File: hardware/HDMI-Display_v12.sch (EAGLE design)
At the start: 105 parts, among them IC1 TFP401A-PAD, IC2 24LC02B, IC3 IS31BL3506A-TTLS2, IC4 ATMEGA32U4-MU, IC5 VREG-TS1117CW-3V3, J20_1 JUMPER2-0402, J20_2 JUMPER2-0402, J30_1 JUMPER2-0402, J30_2 JUMPER2-0402, Q1 16MHz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

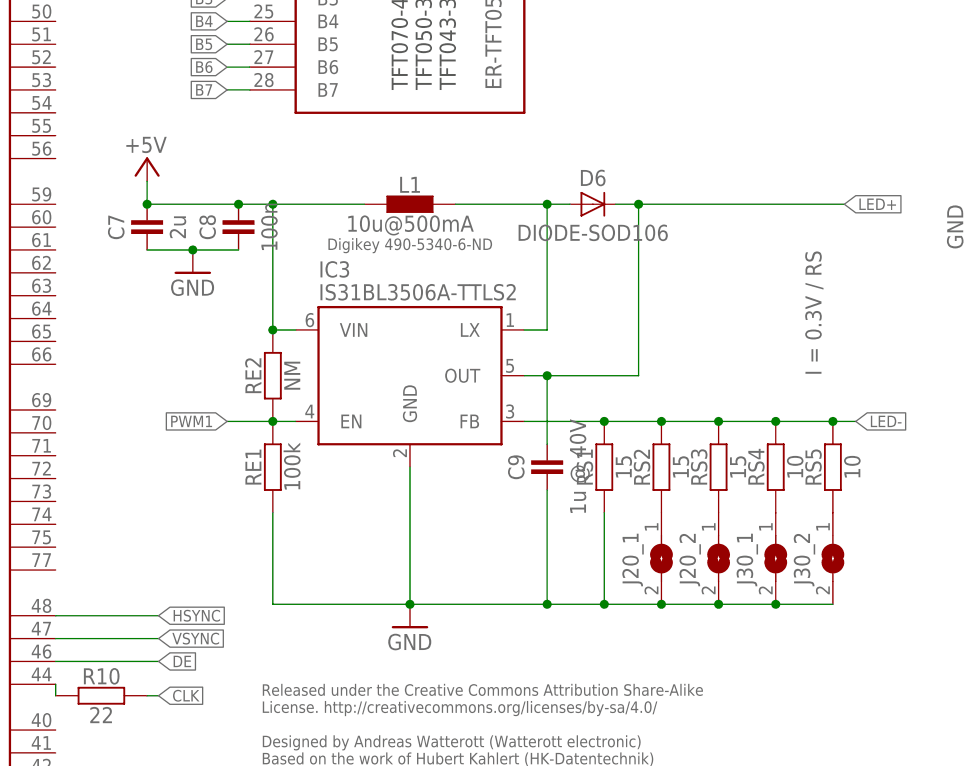
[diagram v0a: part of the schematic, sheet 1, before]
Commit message: updated schematics
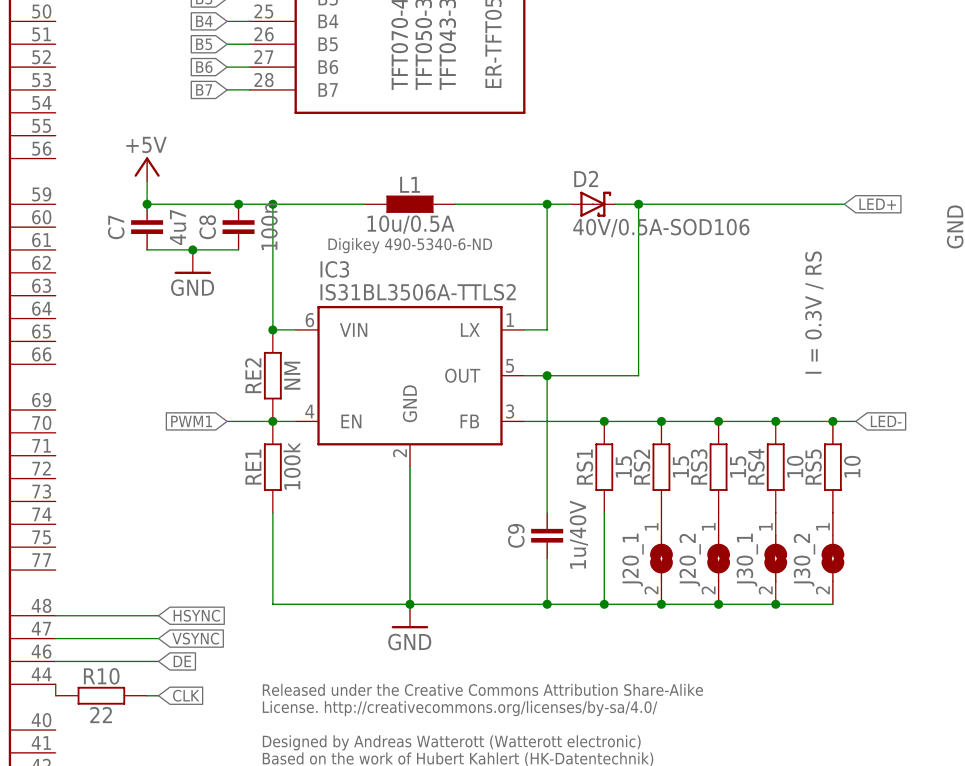
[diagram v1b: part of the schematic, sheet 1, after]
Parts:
- removed D6: DIODE-SOD106, we-rcl:DIODE-SOD106
- added D2: 40V/0.5A-SOD106, we-rcl:D_SCHOTTKY-SOD106
- C7: value 2u -> 4u7
- C9: value 1u @ 40V -> 1u/40V
- L1: value 10u@500mA -> 10u/0.5A
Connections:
- net LED+: now also D2.C; no longer D6.C
- net LX: now also D2.A; no longer D6.A
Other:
- note removed: "Based on the work of Hubert Kahlert (HK-Datentechnik)"
- note removed: "Designed by Andreas Watterott (Watterott electronic)"
- note removed: "Released under the Creative Commons Attribution Share-Alike License"
- note removed: "http://creativecommons.org/licenses/by-sa/4.0/"
- moved on the sheet: C9
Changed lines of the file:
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@@
 <part name="USB" library="we-con" deviceset="USB" device="-MICROB"/>
 <part name="IC3" library="we-power" deviceset="IS31BL3506A" device="-TTLS2"/>
-<part name="L1" library="we-power" deviceset="INDUCTOR" device="-1212" value="10u@500mA"/>
-<part name="D6" library="we-rcl" deviceset="DIODE" device="-SOD106" value="DIODE-SOD106"/>
+<part name="L1" library="we-power" deviceset="INDUCTOR" device="-1212" value="10u/0.5A"/>
 <part name="P+11" library="supply1" deviceset="+5V" device=""/>
 <part name="GND23" library="supply1" deviceset="GND" device=""/>
 <part name="RS2" library="we-rcl" deviceset="RESISTOR" device="-0402" value="15"/>
-<part name="C9" library="we-rcl" deviceset="CAPACITOR" device="-0805" value="1u @ 40V"/>
+<part name="C9" library="we-rcl" deviceset="CAPACITOR" device="-0805" value="1u/40V"/>
 <part name="ISP" library="we-board" deviceset="ISP" device=""/>
 <part name="LCD_TOP" library="we-opto" deviceset="ER-TFT" device="050-3"/>
@@
 <part name="GND9" library="supply1" deviceset="GND" device=""/>
 <part name="C8" library="we-rcl" deviceset="CAPACITOR" device="-0402" value="100n"/>
-<part name="C7" library="we-rcl" deviceset="CAPACITOR" device="-0402" value="2u"/>
+<part name="C7" library="we-rcl" deviceset="CAPACITOR" device="-0402" value="4u7"/>
 <part name="GND6" library="supply1" deviceset="GND" device=""/>
 <part name="RPI" library="we-con" deviceset="MA08-2" device=""/>
@@
 <part name="SW2" library="we-switch" deviceset="SW-2UM" device="-CUS22B"/>
 <part name="SW1" library="we-switch" deviceset="SW-TACTILE" device="-PTS840P"/>
+<part name="D2" library="we-rcl" deviceset="D_SCHOTTKY" device="-SOD106" value="40V/0.5A-SOD106"/>
 </parts>
 <sheets>
@@
 <instance part="IC3" gate="IC" x="179.07" y="57.15"/>
 <instance part="L1" gate="L" x="179.07" y="76.2"/>
-<instance part="D6" gate="D" x="199.39" y="76.2"/>
 <instance part="P+11" gate="1" x="149.86" y="81.28" smashed="yes">
 <attribute name="VALUE" x="147.32" y="81.915" size="1.778" layer="96"/>
@@
 <instance part="GND23" gate="1" x="179.07" y="29.21"/>
 <instance part="RS2" gate="R" x="207.01" y="46.99" rot="R90"/>
-<instance part="C9" gate="C" x="194.31" y="46.99" rot="R90"/>
+<instance part="C9" gate="C" x="194.31" y="39.37" rot="R90"/>
 <instance part="LCD_TOP" gate="LCD" x="179.07" y="128.27"/>
 <instance part="GND44" gate="1" x="201.93" y="160.02"/>
@@
 </instance>
 <instance part="SW2" gate="SW" x="50.8" y="55.88"/>
+<instance part="D2" gate="D" x="199.39" y="76.2"/>
 </instances>
 <busses>
@@
 <segment>
 <pinref part="C9" gate="C" pin="1"/>
-<wire x1="194.31" y1="44.45" x2="194.31" y2="31.75" width="0.1524" layer="91"/>
+<wire x1="194.31" y1="36.83" x2="194.31" y2="31.75" width="0.1524" layer="91"/>
 <junction x="194.31" y="31.75"/>
 <pinref part="IC3" gate="IC" pin="GND"/>
@@
 <wire x1="194.31" y1="57.15" x2="204.47" y2="57.15" width="0.1524" layer="91"/>
 <wire x1="204.47" y1="57.15" x2="204.47" y2="76.2" width="0.1524" layer="91"/>
-<pinref part="D6" gate="D" pin="C"/>
 <wire x1="204.47" y1="76.2" x2="201.93" y2="76.2" width="0.1524" layer="91"/>
 <wire x1="204.47" y1="76.2" x2="227.33" y2="76.2" width="0.1524" layer="91"/>
@@
 <label x="227.33" y="76.2" size="1.27" layer="95" xref="yes"/>
 <pinref part="C9" gate="C" pin="2"/>
-<wire x1="194.31" y1="57.15" x2="194.31" y2="49.53" width="0.1524" layer="91"/>
+<wire x1="194.31" y1="57.15" x2="194.31" y2="41.91" width="0.1524" layer="91"/>
 <junction x="194.31" y="57.15"/>
+<pinref part="D2" gate="D" pin="C"/>
 </segment>
 <segment>
@@
 <pinref part="IC3" gate="IC" pin="LX"/>
 <wire x1="194.31" y1="62.23" x2="191.77" y2="62.23" width="0.1524" layer="91"/>
-<pinref part="D6" gate="D" pin="A"/>
 <wire x1="194.31" y1="76.2" x2="196.85" y2="76.2" width="0.1524" layer="91"/>
 <junction x="194.31" y="76.2"/>
+<pinref part="D2" gate="D" pin="A"/>
 </segment>
 </net>
@@
 <plain>
 <text x="116.84" y="88.9" size="1.778" layer="97">Ambient light sensor</text>
-<text x="162.56" y="21.59" size="1.27" layer="95">Released under the Creative Commons Attribution Share-Alike License</text>
-<text x="162.56" y="19.05" size="1.27" layer="95">http://creativecommons.org/licenses/by-sa/4.0/</text>
-<text x="162.56" y="15.24" size="1.27" layer="95">Designed by Andreas Watterott (Watterott electronic)</text>
-<text x="162.56" y="12.7" size="1.27" layer="95">Based on the work of Hubert Kahlert (HK-Datentechnik)</text>
+<text x="162.56" y="22.86" size="1.27" layer="95" align="top-left">Released under the Creative Commons Attribution Share-Alike
+License. http://creativecommons.org/licenses/by-sa/4.0/
+Designed by Andreas Watterott (Watterott electronic)
+Based on the work of Hubert Kahlert (HK-Datentechnik)</text>
 <text x="99.06" y="76.2" size="1.27" layer="95">A0</text>
 <text x="99.06" y="78.74" size="1.27" layer="95">A1</text>
